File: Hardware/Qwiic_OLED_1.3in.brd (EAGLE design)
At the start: 35.6 x 36.8 mm, 37 parts, among them J1 QWIIC_RIGHT_ANGLE, J2 QWIIC_RIGHT_ANGLE

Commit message: Panelized
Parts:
- moved ADDR 7.12 mm to (17.8, 14.0), turned to 180 degrees
- moved U$4 7.12 mm to (18.5, 14.0)
- moved FID2 1.80 mm to (2.54, 22.9)
- moved FID3 1.80 mm to (2.54, 22.9)
- moved FID1 1.80 mm to (33.0, 2.54)
- moved FID4 1.80 mm to (33.0, 2.54)
- moved C1 1.27 mm to (8.76, 8.89)
- moved C2 1.27 mm to (25.0, 8.89)
- moved C3 1.27 mm to (26.7, 8.89)
- moved C4 1.27 mm to (14.6, 8.89)
- moved C5 1.27 mm to (10.4, 8.89)
- moved C6 1.27 mm to (23.4, 8.89)
- moved C7 1.27 mm to (19.6, 8.89)
- moved OLED 1.27 mm to (17.8, 8.89)
- moved R1 1.27 mm to (12.1, 8.89)
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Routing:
- net D/!C!: track 5.88 -> 11.3 mm, vias 1 -> 2
- net VDD: track 63.5 -> 67.7 mm
- net SCL: track 39.7 -> 41.1 mm
- net SDA: track 50.2 -> 51.5 mm
- net GND: vias 23 -> 25
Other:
- board text added: "Dimensions in Inches"
- board text added: "Route Out"

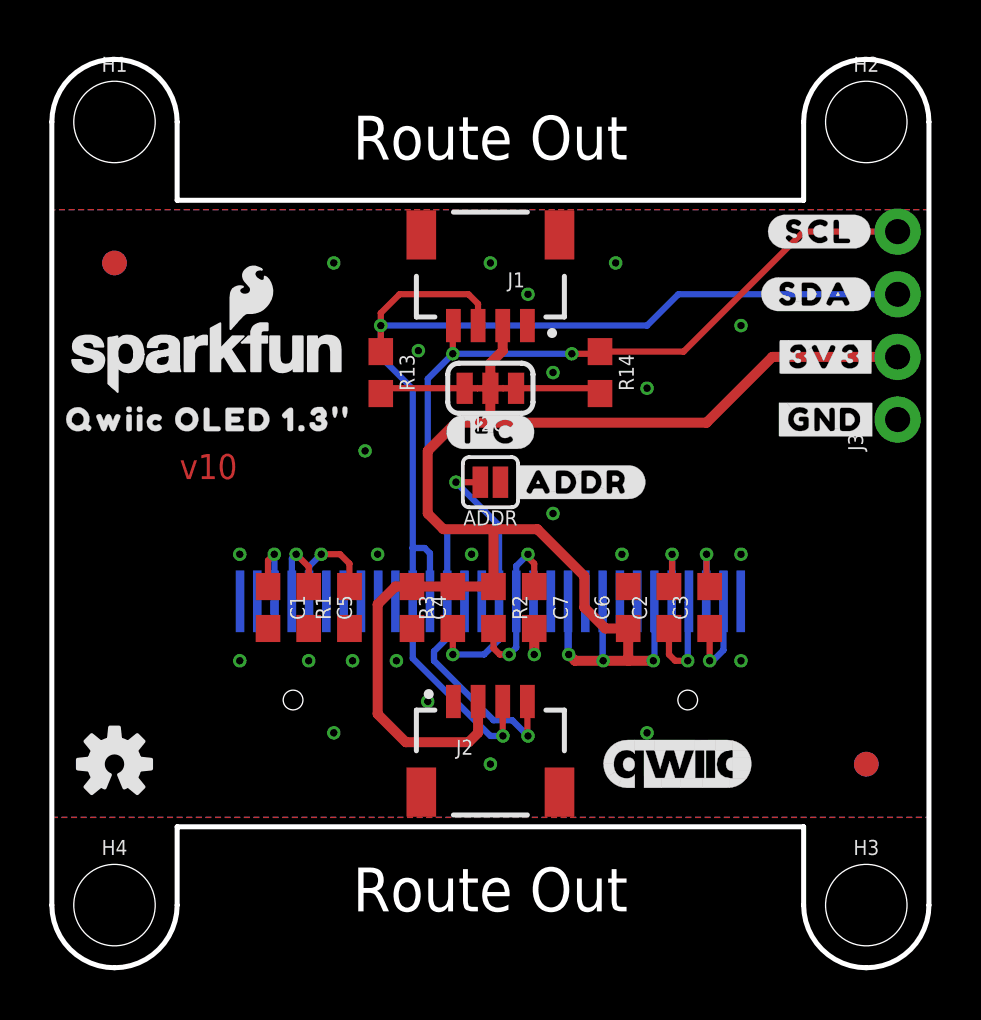
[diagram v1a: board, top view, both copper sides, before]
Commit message: Connect CS to GND
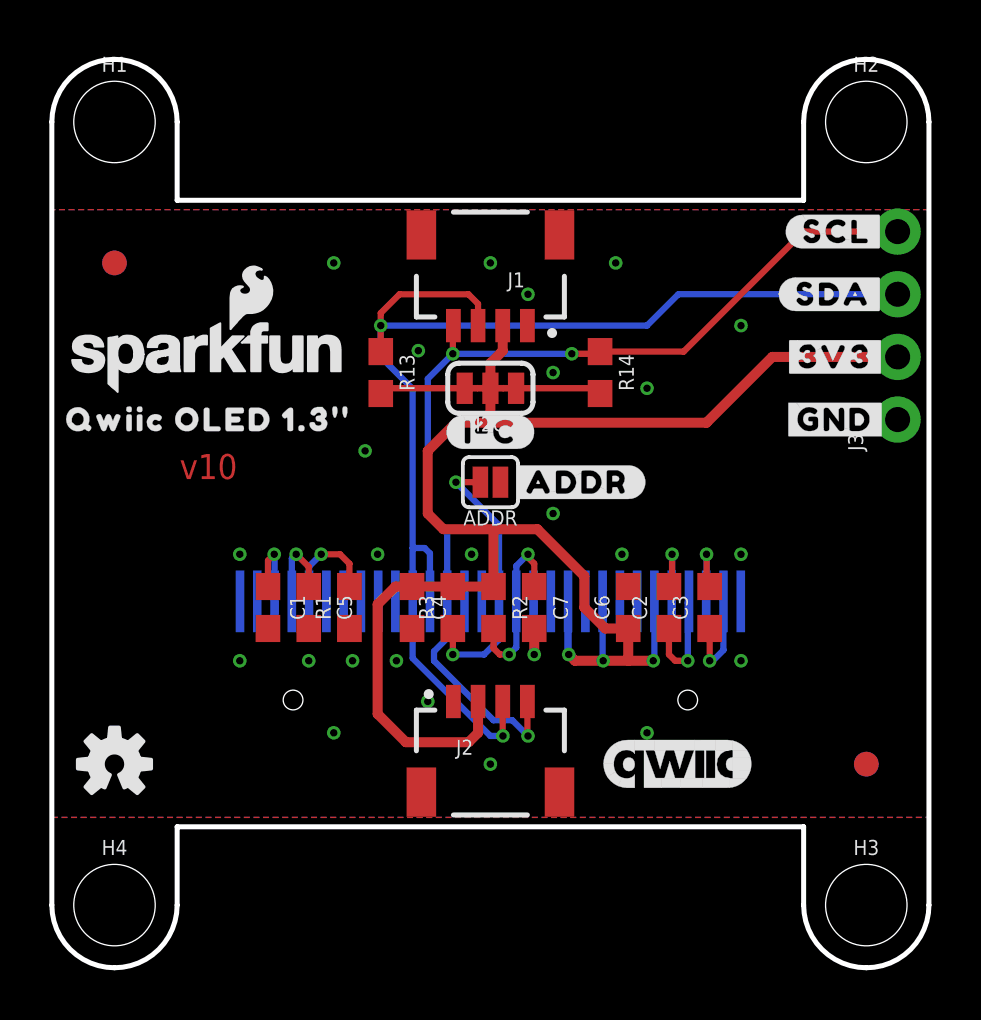
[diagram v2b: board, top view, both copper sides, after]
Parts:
- moved U$7 2.92 mm to (33.9, 21.6)
- moved U$6 2.79 mm to (33.9, 24.1)
- moved U$3 0.38 mm to (31.8, 19.1)
- moved U$5 0.38 mm to (31.8, 16.5)
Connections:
- net GND: now also OLED.13
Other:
- board text removed: "Route Out"
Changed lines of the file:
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@@
 <drawing>
 <settings>
-<setting alwaysvectorfont="yes"/>
+<setting alwaysvectorfont="no"/>
 <setting keepoldvectorfont="yes"/>
 <setting verticaltext="up"/>
 </settings>
-<grid distance="0.05" unitdist="inch" unit="inch" style="lines" multiple="1" display="yes" altdistance="0.005" altunitdist="inch" altunit="inch"/>
+<grid distance="1" unitdist="mm" unit="mm" style="lines" multiple="1" display="yes" altdistance="0.1" altunitdist="mm" altunit="mm"/>
 <layers>
 <layer number="1" name="Top" color="4" fill="1" visible="yes" active="yes"/>
@@
 <wire x1="0.53" y1="1.2" x2="0.53" y2="24.2" width="0.2032" layer="22"/>
 <wire x1="35.03" y1="1.2" x2="35.03" y2="15.24" width="0.2032" layer="22"/>
-<text x="17.78" y="-2.54" size="1.778" layer="20" font="vector" ratio="15" align="center">Route Out</text>
-<text x="17.78" y="27.94" size="1.778" layer="20" font="vector" ratio="15" align="center">Route Out</text>
 <wire x1="13.6" y1="9.4" x2="13.6" y2="8.8" width="0.01" layer="42"/>
 <wire x1="12.9" y1="9.4" x2="12.9" y2="8.8" width="0.01" layer="42"/>
@@
 <text x="-1.27" y="30.48" size="1.778" layer="47" font="vector" ratio="15" align="bottom-right">Dimensions
 in Inches</text>
+<wire x1="19.9" y1="9.4" x2="19.9" y2="8.8" width="0.01" layer="42"/>
 </plain>
 <attributes>
@@
 <element name="C2" library="SparkFun-Capacitors" package="0603" value="1.0uF" x="25.019" y="8.89" smashed="yes" rot="R90">
 <attribute name="NAME" x="24.13" y="8.89" size="0.6096" layer="25" font="vector" ratio="20" rot="R90" align="bottom-center"/>
-<attribute name="PROD_ID" value="CAP-00868" x="25.019" y="8.89" size="1.778" layer="27" rot="R90" display="off"/>
+<attribute name="PROD_ID" value="CAP-13930" x="25.019" y="8.89" size="1.778" layer="27" rot="R90" display="off"/>
 <attribute name="VALUE" x="25.908" y="8.89" size="0.6096" layer="27" font="vector" ratio="20" rot="R90" align="top-center"/>
 </element>
 <element name="C3" library="SparkFun-Capacitors" package="0603" value="1.0uF" x="26.67" y="8.89" smashed="yes" rot="R90">
 <attribute name="NAME" x="25.781" y="8.89" size="0.6096" layer="25" font="vector" ratio="20" rot="R90" align="bottom-center"/>
-<attribute name="PROD_ID" value="CAP-00868" x="26.67" y="8.89" size="1.778" layer="27" rot="R90" display="off"/>
+<attribute name="PROD_ID" value="CAP-13930" x="26.67" y="8.89" size="1.778" layer="27" rot="R90" display="off"/>
 <attribute name="VALUE" x="27.559" y="8.89" size="0.6096" layer="27" font="vector" ratio="20" rot="R90" align="top-center"/>
 </element>
 <element name="C4" library="SparkFun-Capacitors" package="0603" value="1.0uF" x="14.605" y="8.89" smashed="yes" rot="R270">
 <attribute name="NAME" x="15.367" y="8.89" size="0.6096" layer="25" font="vector" ratio="20" rot="R270" align="bottom-center"/>
-<attribute name="PROD_ID" value="CAP-00868" x="14.605" y="8.89" size="1.778" layer="27" rot="R270" display="off"/>
+<attribute name="PROD_ID" value="CAP-13930" x="14.605" y="8.89" size="1.778" layer="27" rot="R270" display="off"/>
 <attribute name="VALUE" x="13.843" y="8.89" size="0.6096" layer="27" font="vector" ratio="20" rot="R270" align="top-center"/>
 </element>
@@
 <element name="C6" library="SparkFun-Capacitors" package="0603" value="1.0uF" x="23.368" y="8.89" smashed="yes" rot="R90">
 <attribute name="NAME" x="22.606" y="8.89" size="0.6096" layer="25" font="vector" ratio="20" rot="R90" align="bottom-center"/>
-<attribute name="PROD_ID" value="CAP-00868" x="23.368" y="8.89" size="1.778" layer="27" rot="R90" display="off"/>
+<attribute name="PROD_ID" value="CAP-13930" x="23.368" y="8.89" size="1.778" layer="27" rot="R90" display="off"/>
 <attribute name="VALUE" x="24.13" y="8.89" size="0.6096" layer="27" font="vector" ratio="20" rot="R90" align="top-center"/>
 </element>
@@
 <element name="C7" library="SparkFun-Capacitors" package="0603" value="1.0uF" x="19.558" y="8.89" smashed="yes" rot="R270">
 <attribute name="NAME" x="20.32" y="8.89" size="0.6096" layer="25" font="vector" ratio="20" rot="R270" align="bottom-center"/>
-<attribute name="PROD_ID" value="CAP-00868" x="19.558" y="8.89" size="1.778" layer="27" font="vector" ratio="15" rot="R270" display="off"/>
+<attribute name="PROD_ID" value="CAP-13930" x="19.558" y="8.89" size="1.778" layer="27" font="vector" ratio="15" rot="R270" display="off"/>
 <attribute name="VALUE" x="18.796" y="8.89" size="0.6096" layer="27" font="vector" ratio="20" rot="R270" align="top-center"/>
 </element>
@@
 <element name="U$1" library="output" package="QWIIC_OLED_1#3##0" value="" x="6.35" y="16.51" smashed="yes"/>
 <element name="U$2" library="output" package="#I�C#2" value="" x="17.78" y="16.002" smashed="yes"/>
-<element name="U$3" library="output" package="#3V3#2" value="" x="31.369" y="19.05" smashed="yes"/>
+<element name="U$3" library="output" package="#3V3#2" value="" x="31.75" y="19.05" smashed="yes"/>
 <element name="U$4" library="output" package="#ADDR#5" value="" x="18.542" y="13.97" smashed="yes"/>
-<element name="U$5" library="output" package="#GND#4" value="" x="31.369" y="16.51" smashed="yes"/>
-<element name="U$6" library="output" package="#SCL#0" value="" x="31.115" y="24.13" smashed="yes"/>
-<element name="U$7" library="output" package="#SDA#1" value="" x="30.988" y="21.59" smashed="yes"/>
+<element name="U$5" library="output" package="#GND#4" value="" x="31.75" y="16.51" smashed="yes"/>
+<element name="U$6" library="output" package="#SCL#0" value="" x="33.909" y="24.13" smashed="yes"/>
+<element name="U$7" library="output" package="#SDA#1" value="" x="33.909" y="21.59" smashed="yes"/>
 <element name="LOGO1" library="SparkFun-Aesthetics" package="QWIIC_6MM" value="QWIIC_LOGO_6MM" x="25.4" y="2.54" smashed="yes"/>
 </elements>
@@
 <via x="20.32" y="12.7" extent="1-16" drill="0.3"/>
 <via x="20.32" y="18.415" extent="1-16" drill="0.3"/>
+<contactref element="OLED" pad="13"/>
 </signal>
 <signal name="VDD">
